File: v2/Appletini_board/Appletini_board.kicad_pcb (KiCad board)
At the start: 4 copper layers, 152.4 x 69.8 mm, 31 parts, among them J1 Conn_02x25_Counter_Clockwise, Q1 TP0610T, U1 SN74LVC543ADW, U10 SN74LVC543ADW, U14 74AHC1G126, U2 Pico, U3 Teensy4.1, U4 SN74LVC543ADW, U5 TXS0108EPW, U6 74LS08, U7 74AHC1G126, U9 SN74LVC543ADW

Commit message: v2 board first draft done
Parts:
- added U8: SN74LVC1G14DBV, Package_TO_SOT_SMD:SOT-23-5, F.Cu at (176.6, 83.1)
- moved R10 104.8 mm to (57.2, 106.1), turned to 0 degrees
- moved R1 75.1 mm to (57.3, 111.3), turned to 180 degrees
- moved R11 64.9 mm to (57.1, 103.6), turned to 0 degrees
- moved C3 45.4 mm to (125.4, 117.4)
- moved R2 18.6 mm to (87.9, 80.7)
- moved JP1 14.5 mm to (176.1, 61.4), turned to 180 degrees
- moved U2 8.54 mm to (72.6, 89.7)
- moved C22 7.45 mm to (190.7, 63.8)
- moved U6 7.24 mm to (187.9, 69.2)
- moved U10 6.21 mm to (166.6, 87.7)
- moved U7 6.21 mm to (171.2, 101.1)
- moved C1 6.21 mm to (161.5, 98.2)
- moved U4 6.21 mm to (147.2, 99.2)
- moved C11 6.21 mm to (132.9, 101.7)
- moved C8 6.21 mm to (109.6, 101.8)
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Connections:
- Q1 pad 3: /VIN -> +5V
- R3 pad 1: /LEVEL_ENABLE -> /Bus transceivers/LEVEL_ENABLE
- U2 pad 21: /PICO_D_~{LEBA} -> /PICO_D_~{OEAB}
- U2 pad 22: /PICO_D_~{OEAB} -> /PICO_D_~{LEBA}
- U2 pad 25: /PICO_~{DMA_CYCLE} -> /PICO_DMA_CYCLE
- U2 pad 32: /LEVEL_ENABLE -> unconnected-(U2-GPIO27_ADC1-Pad32)
- U3 pad 26: /TEENSY_REQ_DMA -> /TEENSY_REQ_~{DMAOUT}
- U3 pad 27: /TEENSY_REQ_~{DMAOUT} -> /TEENSY_REQ_DMA
- U3 pad 4: /~{DMA} -> /TEENSY_CTRL_~{IRQ}
- U3 pad 5: /~{IRQ} -> /PICO_CTRL_~{INH}
- U3 pad 6: /PICO_DMA_CYCLE -> /PICO_CTRL_~{DMA}
- U3 pad 7: /TEENSY_CTRL_~{IRQ} -> /PICO_CTRL_~{RDY}
- U3 pad 9: unconnected-(U3-GPIO7.17-Pad9) -> /PICO_DMA_CYCLE
- U5 pad 10: /LEVEL_ENABLE -> /Bus transceivers/LEVEL_ENABLE
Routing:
- net /PICO_CTRL_~{RDY}: track 0.00 -> 207.9 mm, vias 0 -> 2
- net /PICO_CTRL_~{DMA}: track 0.00 -> 206.3 mm, vias 0 -> 3
- net /PICO_CTRL_~{INH}: track 0.00 -> 199.8 mm, vias 0 -> 2
- net +5V: track 0.00 -> 197.7 mm
- net /PHI0: track 0.00 -> 174.5 mm, vias 0 -> 2
- net /BUS_~{ENABLE}: track 0.00 -> 155.4 mm, vias 0 -> 7
- net /TEENSY_A_~{LEAB}: track 0.00 -> 147.8 mm, vias 0 -> 3
- net /PICO_DMA_CYCLE: track 0.00 -> 140.7 mm, vias 0 -> 1
- net /TEENSY_D_~{LEAB}: track 0.00 -> 139.0 mm, vias 0 -> 1
- net /PICO_A_~{LEBA}: track 0.00 -> 135.2 mm, vias 0 -> 2
- net /TEENSY_A_~{OEBA}: track 0.00 -> 122.8 mm, vias 0 -> 3
- net /PICO_A_~{OEAB}: track 0.00 -> 121.5 mm, vias 0 -> 5
- net /TEENSY_~{INH}: track 0.00 -> 119.2 mm, vias 0 -> 1
- net /PICO_TEENSY_~{IRQ}: track 0.00 -> 109.1 mm, vias 0 -> 1
- net /TEENSY_READY: track 0.00 -> 103.7 mm, vias 0 -> 1
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- added copper zone on In2.Cu, net +3.3V
- added copper zone on B.Cu, net GND
- added copper zone on F.Cu, net GND
- added copper zone on In1.Cu, net GND

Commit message: fixes
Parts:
- removed R10: 10K, Resistor_SMD:R_0402_1005Metric
- removed the U6 at (187.9, 69.2)
- added C14: 100pF, Capacitor_SMD:C_1206_3216Metric, F.Cu at (188.1, 66.0)
- added R2: 10K, Resistor_SMD:R_0402_1005Metric, F.Cu at (185.3, 79.7)
- added R6: 10K, Resistor_SMD:R_0402_1005Metric, F.Cu at (195.9, 77.7)
- added U13: 74LVC1G08, Package_TO_SOT_SMD:SOT-353_SC-70-5, F.Cu at (192.1, 65.8)
- added U8: 74LCX07, Package_SO:TSSOP-14_4.4x5mm_P0.65mm, F.Cu at (191.0, 80.4)
- moved C12 11.3 mm to (191.6, 75.0)
- moved JP1 10.5 mm to (185.9, 57.6)
- renumbered C3 to C1, C7 to C10, C23 to C11, C22 to C12, C1 to C13, C4 to C2, C5 to C3, C6 to C4, C8 to C5, C9 to C6, C10 to C7, C11 to C8, C2 to C9, R11 to R1, R1 to R3, R2 to R4, R3 to R5, U2 to U1, U7 to U10, U8 to U11, U3 to U2, U1 to U3, U10 to U5, U9 to U6, U5 to U7, U14 to U9
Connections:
- net /PICO_DMA_CYCLE renamed /DMA_CYCLE_ACTIVE
- net /PICO_TEENSY_~{IRQ} renamed /TEENSY_~{IRQ}
- U1 pad 13: unconnected-(U2-GND-Pad13) -> GND
- U1 pad 17: /TEENSY_~{INH} -> unconnected-(U1-GPIO13-Pad17)
- U1 pad 18: unconnected-(U2-GND-Pad18) -> GND
- U1 pad 23: unconnected-(U2-GND-Pad23) -> GND
- U1 pad 28: unconnected-(U2-GND-Pad28) -> GND
- U1 pad 29: unconnected-(U2-GPIO22-Pad29) -> /~{DMA}
- U1 pad 3: unconnected-(U2-GND-Pad3) -> GND
- U1 pad 33: unconnected-(U2-AGND-Pad33) -> GND
- U1 pad 38: unconnected-(U2-GND-Pad38) -> GND
- U1 pad 6: /PICO_CTRL_~{DMA} -> unconnected-(U1-GPIO4-Pad6)
- U1 pad 7: /PICO_CTRL_~{INH} -> unconnected-(U1-GPIO5-Pad7)
- U1 pad 8: unconnected-(U2-GND-Pad8) -> GND
- U1 pad 9: /PICO_CTRL_~{RDY} -> unconnected-(U1-GPIO6-Pad9)
- U2 pad 27: /TEENSY_REQ_DMA -> /TEENSY_REQ_~{IRQ}
- U2 pad 4: /TEENSY_CTRL_~{IRQ} -> /TEENSY_REQ_DMA
- U2 pad 5: /PICO_CTRL_~{INH} -> /~{INH}
- U2 pad 6: /PICO_CTRL_~{DMA} -> /~{DMA}
- U2 pad 7: /PICO_CTRL_~{RDY} -> /~{RDY}
- U2 pad 8: /TEENSY_~{INH} -> unconnected-(U2-GPIO7.10-Pad8)
- U7 pad 3: /Bus transceivers/CTRL_~{DMAOUT} -> /Bus transceivers/~{DMAOUT}
- U7 pad 4: /Bus transceivers/CTRL_~{INTOUT} -> /Bus transceivers/~{INTOUT}
- U7 pad 5: /PICO_CTRL_~{DMA} -> /~{DMA}
- U7 pad 6: /PICO_CTRL_~{RDY} -> /~{RDY}
- U7 pad 7: /TEENSY_CTRL_~{IRQ} -> /Bus transceivers/~{IRQ}
- U7 pad 8: /PICO_CTRL_~{INH} -> /~{INH}
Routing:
- net /PICO_CTRL_~{RDY}: track 207.9 -> 0.00 mm, vias 2 -> 0
- net /PICO_CTRL_~{DMA}: track 206.3 -> 0.00 mm, vias 3 -> 0
- net /PICO_CTRL_~{INH}: track 199.8 -> 0.00 mm, vias 2 -> 0
- net /~{DMA}: track 0.00 -> 193.5 mm, vias 0 -> 3
- net /TEENSY_~{INH}: track 119.2 -> 0.00 mm, vias 1 -> 0
- net /TEENSY_REQ_~{IRQ}: track 0.00 -> 78.6 mm
- net /~{RDY}: track 0.00 -> 69.0 mm, vias 0 -> 2
- net /TEENSY_CTRL_~{IRQ}: track 65.6 -> 0.00 mm
- net /~{INH}: track 0.00 -> 62.3 mm, vias 0 -> 2
- net /TEENSY_REQ_DMA: track 69.8 -> 37.7 mm
- net /Bus transceivers/CTRL_~{DMAOUT}: track 30.0 -> 0.00 mm, vias 2 -> 0
- net /Bus transceivers/CTRL_~{INTOUT}: track 24.6 -> 0.00 mm
- net /TEENSY_REQ_~{DMAOUT}: track 72.1 -> 95.1 mm
- net /Bus transceivers/~{INTOUT}: track 0.00 -> 18.4 mm
- net /Bus transceivers/~{DMAOUT}: track 0.00 -> 17.7 mm
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
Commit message: pcb debugging, first draft of PIO
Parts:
- removed U1: Pico, RPi_Pico:RPi_Pico_SMD_TH
- removed U2: Teensy4.1, teensy:Teensy41
- added J2: Conn_01x20, Connector_PinSocket_2.54mm:PinSocket_1x20_P2.54mm_Vertical, F.Cu at (63.7, 65.5)
- added J3: Conn_01x20, Connector_PinSocket_2.54mm:PinSocket_1x20_P2.54mm_Vertical, F.Cu at (81.5, 113.8)
- added J4: Conn_01x24, Connector_PinSocket_2.54mm:PinSocket_1x24_P2.54mm_Vertical, F.Cu at (113.0, 73.6)
- added J5: Conn_01x24, Connector_PinSocket_2.54mm:PinSocket_1x24_P2.54mm_Vertical, F.Cu at (171.4, 58.3)
- moved R3 45.9 mm to (58.1, 65.4)
- moved R1 32.8 mm to (87.4, 90.8), turned to 180 degrees
- moved C1 2.40 mm to (124.6, 115.2)
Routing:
- net /TEENSY_~{IRQ}: track 109.1 -> 58.0 mm
- net /TEENSY_READY: track 103.7 -> 60.3 mm, vias 1 -> 0
- net /TEENSY_~{EMIT_DATA}: track 78.0 -> 54.4 mm
- net /DMA_CYCLE_ACTIVE: track 146.3 -> 157.0 mm, vias 1 -> 2
- net /~{DMA}: track 193.5 -> 201.3 mm
- net /PICO_D_~{LEBA}: track 31.7 -> 27.5 mm
- net /PICO_A_~{OEAB}: track 121.5 -> 119.4 mm, vias 5 -> 6
- net +12V: track 9.26 -> 11.1 mm
- net /BUS_D4: track 59.6 -> 58.4 mm
- net /PICO_D_~{OEAB}: track 22.1 -> 21.0 mm
- net /PICO_A_~{LEBA}: track 135.2 -> 136.2 mm
- net /PHI0: track 174.5 -> 173.9 mm
- net GND: track 95.4 -> 95.7 mm, vias 27 -> 26

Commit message: checkpoint before lvc573 rework
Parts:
- C1, C10, C11, C12, C13, C14, C2, C3, C4, C5, C6, C7, C8, C9: value 100pF -> 100nF
- U10, U13, U9: footprint Package_TO_SOT_SMD:SOT-353_SC-70-5 -> Package_TO_SOT_SMD:SOT-23-5
- moved C13 0.73 mm to (161.3, 97.5)
- moved U10 0.59 mm to (171.6, 101.7)
- moved C10 0.41 mm to (168.6, 97.6)
- moved C14 0.37 mm to (187.8, 66.1)
- moved U9 0.25 mm to (164.0, 101.7)
- moved J1 0.22 mm to (161.8, 123.0)
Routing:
- net /BUS_R~{W}: track 40.5 -> 37.8 mm
- net /PICO_A_~{OEAB}: track 119.4 -> 121.8 mm
- net GND: track 95.7 -> 96.9 mm
- net +3.3V: track 63.6 -> 64.6 mm
- net /BUS_M2B0: track 23.0 -> 22.5 mm
- net /DMA_CYCLE_ACTIVE: track 157.0 -> 157.6 mm
- net /TEENSY_REQ_DMA: track 37.7 -> 37.2 mm
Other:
- outline, holes or cut-outs redrawn

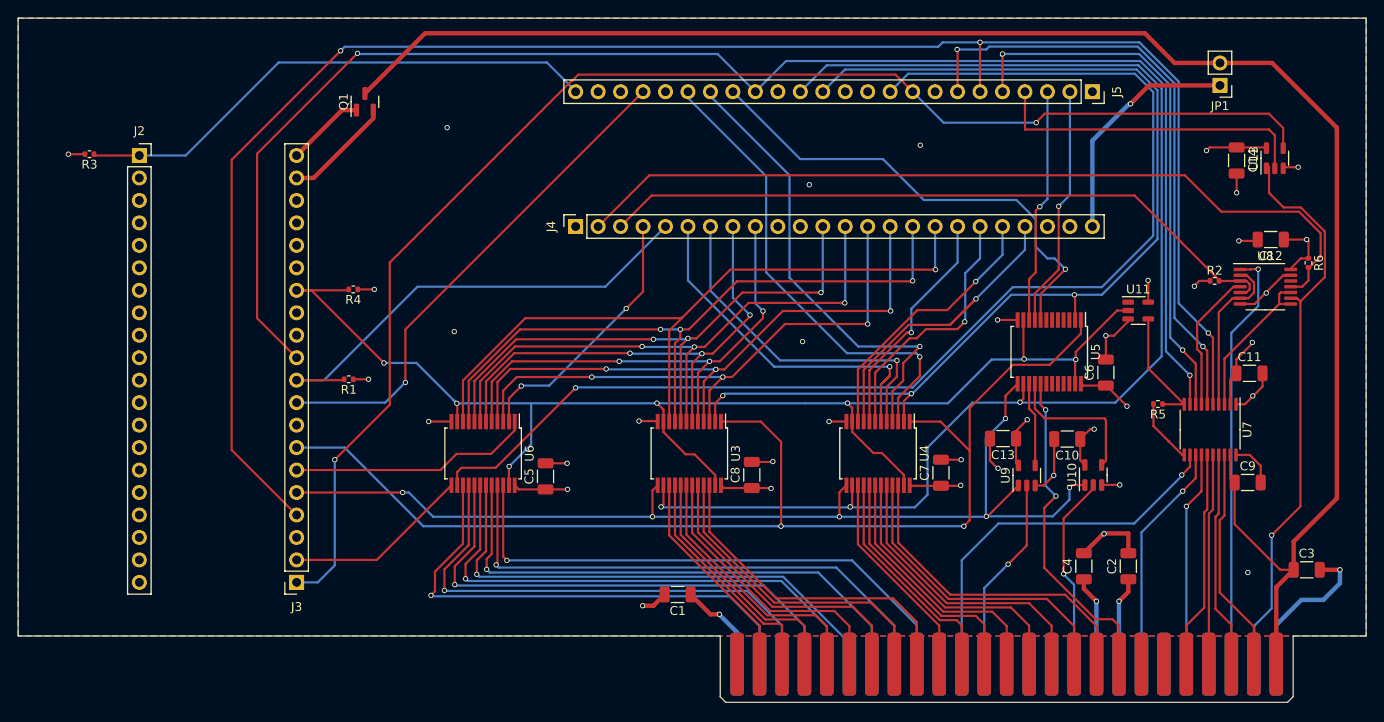
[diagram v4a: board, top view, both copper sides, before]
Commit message: board ordered
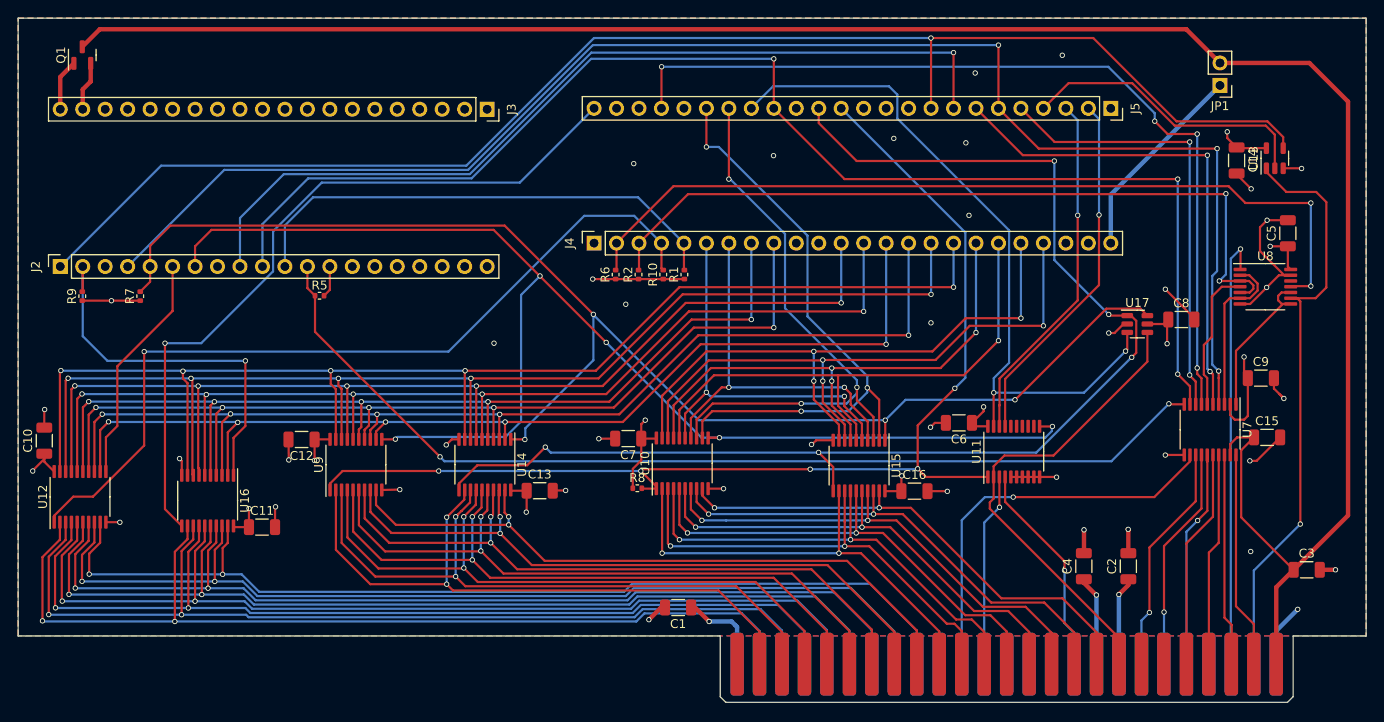
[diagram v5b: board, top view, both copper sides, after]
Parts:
- removed R3, R4: 10K, Resistor_SMD:R_0402_1005Metric
- removed U3, U4, U5, U6: SN74LVC543ADW, Package_SO:SSOP-24_5.3x8.2mm_P0.65mm
- added C15: 100nF, Capacitor_SMD:C_1206_3216Metric, F.Cu at (191.2, 97.4)
- added C16: 100nF, Capacitor_SMD:C_1206_3216Metric, F.Cu at (151.3, 103.5)
- added R10: 10K, Resistor_SMD:R_0402_1005Metric, F.Cu at (122.9, 79.0)
- added R7: 10K, Resistor_SMD:R_0402_1005Metric, F.Cu at (63.8, 81.4)
- added R8: 10K, Resistor_SMD:R_0402_1005Metric, F.Cu at (120.0, 103.2)
- added R9: 10K, Resistor_SMD:R_0402_1005Metric, F.Cu at (57.3, 81.4)
- added U12: 74LS573, Package_SO:TSSOP-20_4.4x6.5mm_P0.65mm, F.Cu at (57.0, 104.1)
- added U14: 74LS573, Package_SO:TSSOP-20_4.4x6.5mm_P0.65mm, F.Cu at (102.8, 100.5)
- added U15: 74LS573, Package_SO:TSSOP-20_4.4x6.5mm_P0.65mm, F.Cu at (145.1, 100.6)
- added U16: 74LS573, Package_SO:TSSOP-20_4.4x6.5mm_P0.65mm, F.Cu at (71.4, 104.5)
- added U17: 74LVC1G373, Package_TO_SOT_SMD:SOT-23-6, F.Cu at (176.5, 84.6)
- U10, U9: value 74AHC1G126 -> 74LS573; footprint Package_TO_SOT_SMD:SOT-23-5 -> Package_SO:TSSOP-20_4.4x6.5mm_P0.65mm
- U11: value SN74LVC1G14DBV -> 74LS573; footprint Package_TO_SOT_SMD:SOT-23-5 -> Package_SO:TSSOP-20_4.4x6.5mm_P0.65mm
- moved C10 115.6 mm to (53.0, 97.8), turned to 90 degrees
- moved C11 113.0 mm to (77.6, 107.5)
- moved C12 111.9 mm to (82.0, 97.6)
- moved R5 95.6 mm to (84.1, 81.4), turned to 0 degrees
- moved C5 88.3 mm to (193.5, 74.3)
- moved R6 78.3 mm to (117.6, 79.0), turned to 90 degrees
- moved U9 75.9 mm to (88.2, 100.5)
- moved R2 65.1 mm to (120.1, 79.0), turned to 90 degrees
- moved J3 57.7 mm to (103.0, 60.3), turned to -90 degrees
- moved C13 52.7 mm to (109.0, 103.4), turned to 0 degrees
- moved C8 51.6 mm to (181.5, 84.1), turned to 0 degrees
- moved U10 46.5 mm to (125.1, 100.3)
- moved R1 39.7 mm to (125.3, 79.0), turned to 90 degrees
- moved C7 35.6 mm to (119.0, 97.5), turned to 180 degrees
- moved Q1 32.4 mm to (57.3, 54.2)
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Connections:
- C9 pad 1: +5V -> +3.3V
- J1 pad 31: unconnected-(J1-Pin_31-Pad31) -> /BUS_~{RES}
- J2 pad 1: /TEENSY_READY -> /DMA_CYCLE_ACTIVE
- J2 pad 10: unconnected-(J2-Pin_10-Pad10) -> /PHI0
- J2 pad 11: unconnected-(J2-Pin_11-Pad11) -> /TEENSY_~{EMIT_DATA}
- J2 pad 12: unconnected-(J2-Pin_12-Pad12) -> /LEVEL_ENABLE
- J2 pad 2: unconnected-(J2-Pin_2-Pad2) -> /DATA_TX_~{ENABLE}
- J2 pad 4: unconnected-(J2-Pin_4-Pad4) -> /~{DMA}
- J2 pad 5: unconnected-(J2-Pin_5-Pad5) -> /ADDR_TX_~{ENABLE}
- J2 pad 6: unconnected-(J2-Pin_6-Pad6) -> /DATA_RX_LATCH
- J2 pad 7: unconnected-(J2-Pin_7-Pad7) -> /ADDR_RX_LATCH
- J2 pad 9: unconnected-(J2-Pin_9-Pad9) -> /TEENSY_~{IRQ}
- J3 pad 1: /DMA_CYCLE_ACTIVE -> unconnected-(J3-Pin_1-Pad1)
- J3 pad 10: /TEENSY_~{EMIT_DATA} -> unconnected-(J3-Pin_10-Pad10)
- J3 pad 11: /PHI0 -> unconnected-(J3-Pin_11-Pad11)
- J3 pad 14: /BUS_~{ENABLE} -> unconnected-(J3-Pin_14-Pad14)
- J3 pad 2: /PICO_D_~{OEAB} -> unconnected-(J3-Pin_2-Pad2)
- J3 pad 4: /~{DMA} -> unconnected-(J3-Pin_4-Pad4)
- J3 pad 5: /PICO_A_~{OEAB} -> unconnected-(J3-Pin_5-Pad5)
- J3 pad 6: /PICO_D_~{LEBA} -> unconnected-(J3-Pin_6-Pad6)
- J3 pad 7: /PICO_A_~{LEBA} -> unconnected-(J3-Pin_7-Pad7)
- J3 pad 9: /TEENSY_~{IRQ} -> unconnected-(J3-Pin_9-Pad9)
- J4 pad 12: /Bus transceivers/B2 -> /B2
- J4 pad 13: /Bus transceivers/B3 -> /B3
- J4 pad 14: /Bus transceivers/B7 -> /B7
- J4 pad 15: /Bus transceivers/B6 -> /B6
- J4 pad 16: /Bus transceivers/B1 -> /B1
- J4 pad 17: /Bus transceivers/B0 -> /B0
- J4 pad 18: /Bus transceivers/B10 -> /B10
- J4 pad 19: /Bus transceivers/B11 -> /B11
- J4 pad 20: /Bus transceivers/B8 -> /B8
- J4 pad 21: /Bus transceivers/B9 -> /B9
- J4 pad 4: /TEENSY_D_~{OEBA} -> /DATA_RX_~{ENABLE}
- J4 pad 6: /Bus transceivers/B12 -> /B12
- J4 pad 7: /Bus transceivers/B13 -> /B13
- J4 pad 8: /Bus transceivers/B4 -> /B4
- J4 pad 9: /Bus transceivers/B5 -> /B5
- J5 pad 10: /TEENSY_D_~{LEAB} -> unconnected-(J5-Pin_10-Pad10)
- J5 pad 13: /TEENSY_A_~{OEBA} -> /ADDR_RX_~{ENABLE}
- J5 pad 14: /TEENSY_A_~{LEAB} -> /ADDR_TX_LATCH
- J5 pad 18: /Bus transceivers/B14 -> /B14
- J5 pad 19: /Bus transceivers/B15 -> /B15
- J5 pad 21: /TEENSY_~{IRQ} -> /~{RES}
- J5 pad 24: /TEENSY_READY -> /DATA_TX_LATCH
- J5 pad 8: unconnected-(J5-Pin_8-Pad8) -> /TEENSY_~{IRQ}
- R5 pad 1: /Bus transceivers/LEVEL_ENABLE -> /LEVEL_ENABLE
- U10 pad 1: /PICO_A_~{OEAB} -> /ADDR_RX_~{ENABLE}
- U10 pad 2: /BUS_M2B0 -> /BUS_A8
- U10 pad 3: GND -> /BUS_A9
- U10 pad 4: /Bus transceivers/BUF_M2B0 -> /BUS_A10
- U10 pad 5: +3.3V -> /BUS_A11
- U11 pad 1: unconnected-(U11-NC-Pad1) -> /ADDR_RX_~{ENABLE}
- U11 pad 2: /BUS_~{ENABLE} -> /BUS_R~{W}
- U11 pad 3: GND -> /BUS_M2SEL
- U11 pad 4: /Bus transceivers/LEVEL_ENABLE -> /BUS_M2B0
- U11 pad 5: +3.3V -> GND
- U7 pad 1: GND -> /Bus transceivers/~{DMAOUT}
- U7 pad 10: /Bus transceivers/LEVEL_ENABLE -> /LEVEL_ENABLE
- U7 pad 14: /BUS_~{IRQ} -> /BUS_~{RES}
- U7 pad 15: /BUS_~{RDY} -> /BUS_~{IRQ}
- U7 pad 16: /BUS_~{DMA} -> /BUS_~{RDY}
- U7 pad 17: /BUS_~{INTOUT} -> /BUS_~{DMA}
- U7 pad 18: /BUS_~{DMAOUT} -> /BUS_~{INTOUT}
- U7 pad 20: GND -> /BUS_~{DMAOUT}
- U7 pad 3: /Bus transceivers/~{DMAOUT} -> /Bus transceivers/~{INTOUT}
- U7 pad 4: /Bus transceivers/~{INTOUT} -> /~{DMA}
- U7 pad 5: /~{DMA} -> /~{RDY}
- U7 pad 6: /~{RDY} -> /Bus transceivers/~{IRQ}
- U7 pad 7: /Bus transceivers/~{IRQ} -> /~{RES}
- U9 pad 1: /PICO_A_~{OEAB} -> /ADDR_RX_~{ENABLE}
- U9 pad 2: /BUS_M2SEL -> /BUS_A0
- U9 pad 3: GND -> /BUS_A1
- U9 pad 4: /Bus transceivers/BUF_M2SEL -> /BUS_A2
- U9 pad 5: +3.3V -> /BUS_A3
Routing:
- net /ADDR_TX_~{ENABLE}: track 0.00 -> 155.4 mm, vias 0 -> 4
- net /BUS_~{ENABLE}: track 155.4 -> 0.00 mm, vias 7 -> 0
- net /B0: track 0.00 -> 149.1 mm, vias 0 -> 5
- net /TEENSY_A_~{LEAB}: track 147.8 -> 0.00 mm, vias 3 -> 0
- net /ADDR_RX_LATCH: track 0.00 -> 147.5 mm, vias 0 -> 5
- net /ADDR_TX_LATCH: track 0.00 -> 146.0 mm, vias 0 -> 5
- net /B1: track 0.00 -> 143.0 mm, vias 0 -> 5
- net /TEENSY_D_~{LEAB}: track 139.0 -> 0.00 mm, vias 1 -> 0
- net /PICO_A_~{LEBA}: track 136.2 -> 0.00 mm, vias 2 -> 0
- net /ADDR_RX_~{ENABLE}: track 0.00 -> 129.5 mm, vias 0 -> 5
- net /B2: track 0.00 -> 129.4 mm, vias 0 -> 5
- net /B3: track 0.00 -> 128.5 mm, vias 0 -> 5
- net /B6: track 0.00 -> 125.5 mm, vias 0 -> 5
- net /TEENSY_A_~{OEBA}: track 122.8 -> 0.00 mm, vias 3 -> 0
- net /PICO_A_~{OEAB}: track 121.8 -> 0.00 mm, vias 6 -> 0
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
